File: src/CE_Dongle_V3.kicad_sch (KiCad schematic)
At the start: 6 parts, among them J2 8P8C_LED_Shielded

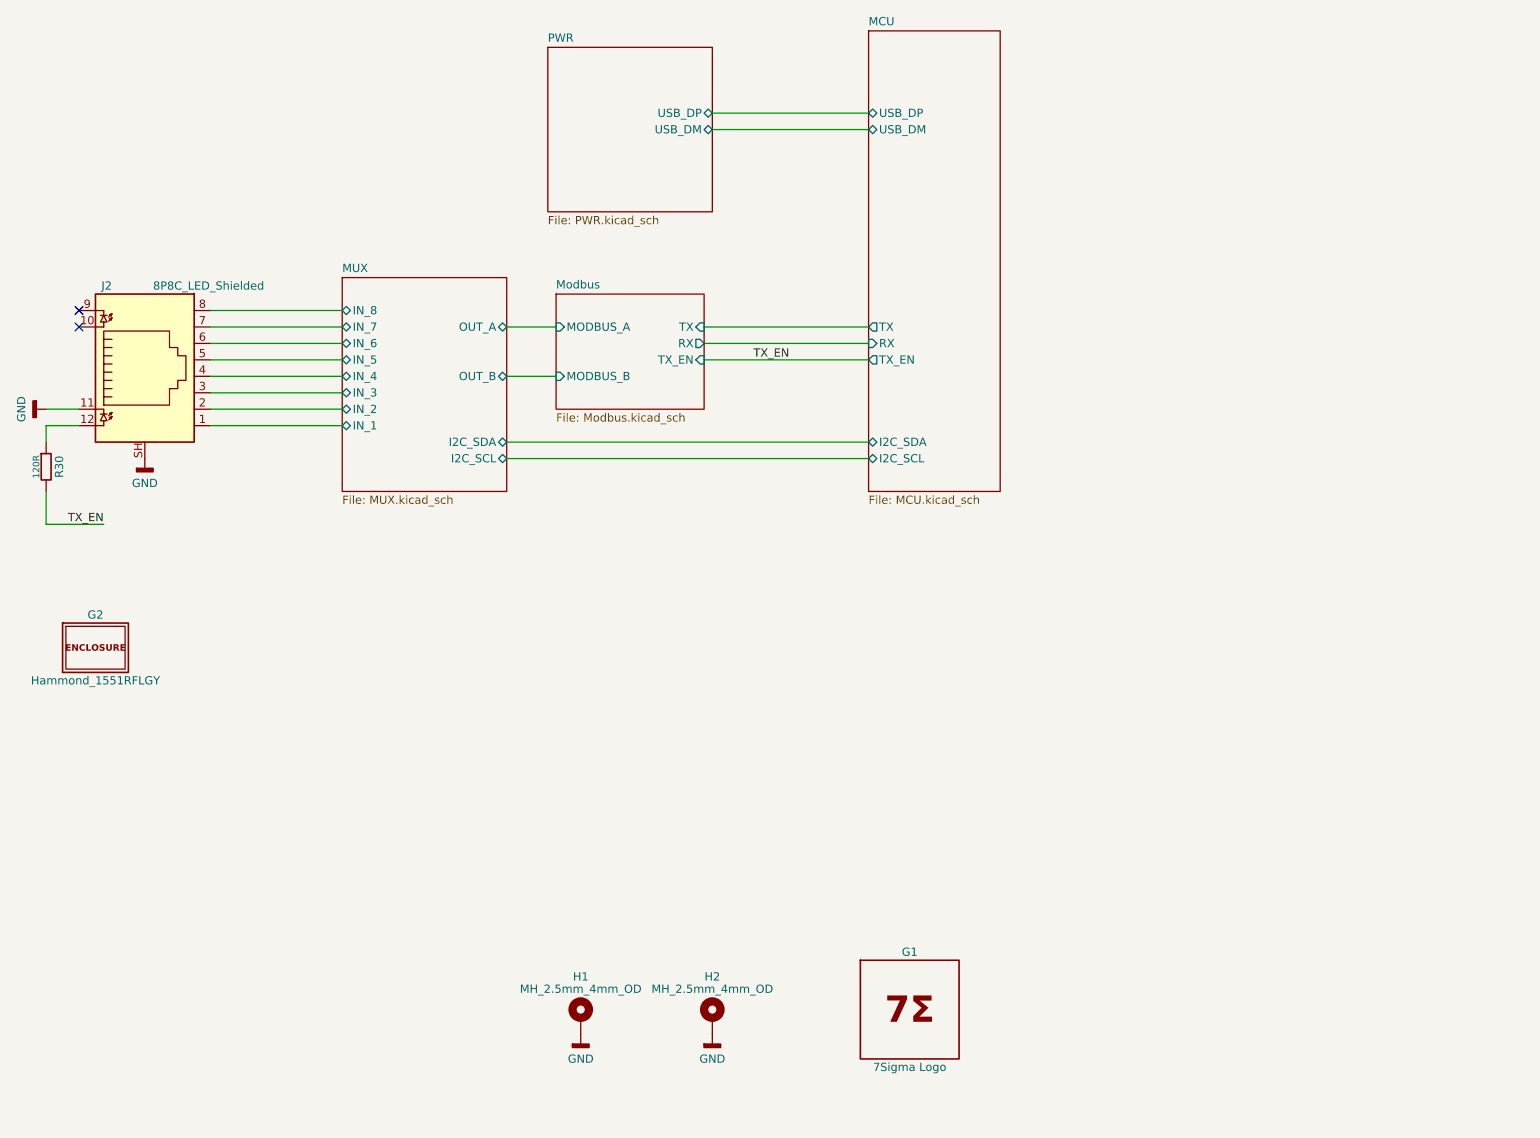
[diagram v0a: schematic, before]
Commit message: V3.1 first changes
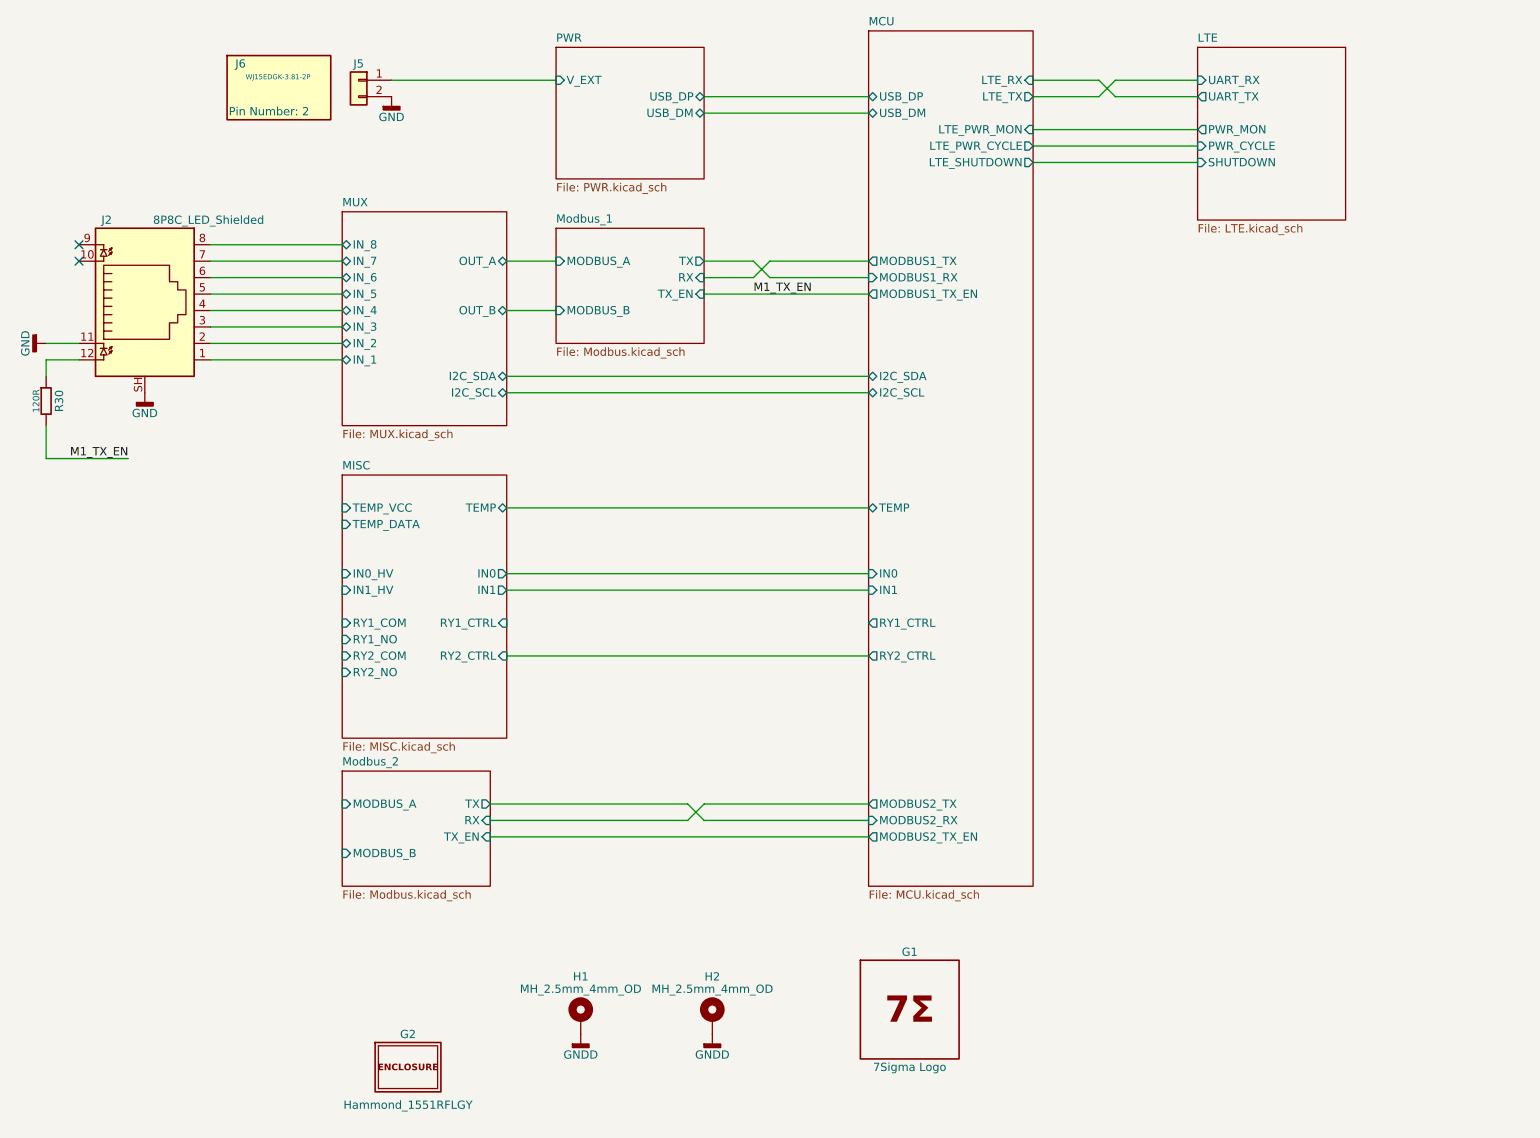
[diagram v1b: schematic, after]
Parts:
- added J5: Conn_01x02, 7Sigma:PhoenixContact_MC_1,5_2-G-3.81_1x02_P3.81mm_Horizontal, symbol Connectors:WJ15EDGRC-3.81-2P
- added J6: WJ15EDGK-3.81-2P, 7Sigma:TerminalBlock_Plug_Invisible, symbol Connectors:WJ15EDGK-3.81-2P
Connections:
- net GND: now also J5.2 (Pin_2); no longer H1.1, H2.1
- net TX_EN renamed M1_TX_EN
- new net GNDD: H1.1, H2.1
- new net PWR/V_EXT: J5.1 (Pin_1)
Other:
- sheet Modbus renamed Modbus_1
- added sheet LTE (LTE.kicad_sch)
- added sheet MISC (MISC.kicad_sch)
- added sheet Modbus_2 (Modbus.kicad_sch)
- sheet MCU ports: added IN0, IN1, LTE_PWR_CYCLE, LTE_PWR_MON, LTE_RX, LTE_SHUTDOWN, LTE_TX, MODBUS1_RX, MODBUS1_TX, MODBUS1_TX_EN, MODBUS2_RX, MODBUS2_TX, MODBUS2_TX_EN, RY1_CTRL, RY2_CTRL, TEMP; removed RX, TX, TX_EN
- sheet PWR ports: added V_EXT; removed none
- moved on the sheet: G2, J2, R30

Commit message: ongoing work
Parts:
- removed G2: Hammond_1551RFLGY, 7Sigma:HAMMOND_1551RFLGY, symbol Mechanical_7S:Hammond_1551RFLGY
- removed J2: 8P8C_LED_Shielded, 7Sigma:RJ45-TH_RC01812, symbol Connectors:RC01812
- removed J5: Conn_01x02, 7Sigma:PhoenixContact_MC_1,5_2-G-3.81_1x02_P3.81mm_Horizontal, symbol Connectors:WJ15EDGRC-3.81-2P
- removed J6: WJ15EDGK-3.81-2P, 7Sigma:TerminalBlock_Plug_Invisible, symbol Connectors:WJ15EDGK-3.81-2P
- removed R30: 120R, 7Sigma:R_0402_1005Metric, symbol Resistor:0402WGF1200TCE
- added ENC1: Hammond_1551XFLGY, 7Sigma:HAMMOND_1551XFLGY, symbol Mechanical_7S:Hammond_1551XFLGY
- added H3, H4: MH_2.5mm_4mm_OD, 7Sigma:MountingHole_2.5mm_Pad_4mm, symbol Mechanical_7S:MH_2.5mm_4mm_OD
- added J6: DB2EKDM-3.81-10P-GN, 7Sigma:TerminalBlock_Plug_Invisible, symbol Connectors:DB2EKDM-3.81-10P-GN
- added J7: 8P8C_LED_Shielded, 7Sigma:RJ45-TH_RC01812, symbol Connectors:RC01812
- added J8: DB2ERM-3.81-10P-GN, 7Sigma:PhoenixContact_MC_1,5_10-GF-3.81_1x10_P3.81mm_Horizontal_ThreadedFlange, symbol Connectors:DB2ERM-3.81-10P-GN
- added R29: 1K, 7Sigma:R_0402_1005Metric, symbol Resistor:0402WGF1001TCE
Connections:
- net GNDD is gone; now on net GND: H1.1, H2.1
- net GND: now also H3.1, H4.1, J7.SH, J8.3 (Pin_3), J8.8 (Pin_8), R29.2
- net MISC/RY1_COM: now also J8.4 (Pin_4)
- net MISC/RY1_NO: now also J8.5 (Pin_5)
- net MISC/RY2_NO: now also J8.6 (Pin_6)
- net MISC/TEMP_DATA: now also J8.2 (Pin_2)
- net MISC/TEMP_VCC: now also J8.1 (Pin_1)
- net MUX/IN_1: now also J7.1
- net MUX/IN_2: now also J7.2
- net MUX/IN_3: now also J7.3
- net MUX/IN_4: now also J7.4
- net MUX/IN_5: now also J7.5
- net MUX/IN_6: now also J7.6
- net MUX/IN_7: now also J7.7
- net MUX/IN_8: now also J7.8
- net MUX/OUT_A: now also J8.9 (Pin_9)
- net MUX/OUT_B: now also J8.10 (Pin_10)
- net PWR/V_EXT: now also J8.7 (Pin_7)
- new net: J7.11, R29.1
- new net TX_EN: J7.12
- no-connect marks 2 -> 0
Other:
- removed sheet Modbus_2
- sheet MCU ports: added none; removed IN0, IN1, MODBUS2_RX, MODBUS2_TX, MODBUS2_TX_EN
- sheet MISC ports: added R1_CTRL, R2_CTRL; removed IN0, IN0_HV, IN1, IN1_HV, RY1_CTRL, RY2_CTRL
- moved on the sheet: G1, H1, H2

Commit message: Layout progress
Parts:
- removed J6: DB2EKDM-3.81-10P-GN, 7Sigma:TerminalBlock_Plug_Invisible, symbol Connectors:DB2EKDM-3.81-10P-GN
- removed J8: DB2ERM-3.81-10P-GN, 7Sigma:PhoenixContact_MC_1,5_10-GF-3.81_1x10_P3.81mm_Horizontal_ThreadedFlange, symbol Connectors:DB2ERM-3.81-10P-GN
- added J10, J2, J3, J6, J8: Conn_01x02, 7Sigma:CONN-TH_DB301V-3.5-2P-GN, symbol Connectors:DB301V-3.5-2P-GN-S
- ENC1: Manufacturer 1 (none) -> FIX&Hammond Mfg; Manufacturer Part Number 1 (none) -> 1551XFLGY; Price @Bulk USD (none) -> 2.3700; Price Source (none) -> Manual
- J7: Price @1 USD (none) -> 0.5973; Price @100 USD (none) -> 0.3342; Price @Bulk USD (none) -> 0.2890; Price Bulk Qty (none) -> 1000; Price Source (none) -> LCSC; Price Updated (none) -> 2026-05-14
- R29: Price @1 USD (none) -> 0.0011; Price @100 USD (none) -> 0.0011; Price @Bulk USD (none) -> 0.0009; Price Bulk Qty (none) -> 1000; Price Source (none) -> LCSC; Price Updated (none) -> 2026-05-14
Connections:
- net GND: now also J3.1 (Pin_1), J8.2 (Pin_2)
- net MISC/RY1_COM: now also J3.2 (Pin_2)
- net MISC/RY1_NO: now also J6.1 (Pin_1)
- net MISC/RY2_NO: now also J6.2 (Pin_2)
- net MISC/TEMP_DATA: now also J2.2 (Pin_2)
- net MISC/TEMP_VCC: now also J2.1 (Pin_1)
- net MUX/OUT_A: now also J10.1 (Pin_1)
- net MUX/OUT_B: now also J10.2 (Pin_2)
- net PWR/V_EXT: now also J8.1 (Pin_1)

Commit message: PCB layout continued
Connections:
- net MISC/RY1_COM: now also J6.1 (Pin_1); no longer J3.2 (Pin_2)
- net MISC/RY1_NO: now also J3.2 (Pin_2); no longer J6.1 (Pin_1)
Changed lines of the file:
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@@
 	(paper "A4")
 	(junction
-		(at 101.6 66.04)
+		(at 127 104.14)
 		(diameter 0)
 		(color 0 0 0 0)
 	)
 	(junction
-		(at 127 101.6)
+		(at 101.6 66.04)
 		(diameter 0)
 		(color 0 0 0 0)
@@
 	(wire
 		(pts
-			(xy 129.54 104.14) (xy 127 104.14)
+			(xy 129.54 106.68) (xy 127 106.68)
 		)
 		(stroke
@@
 	(wire
 		(pts
-			(xy 127 101.6) (xy 129.54 101.6)
+			(xy 127 104.14) (xy 129.54 104.14)
 		)
 		(stroke
@@
 	(wire
 		(pts
-			(xy 139.7 60.96) (xy 162.56 60.96)
+			(xy 86.36 101.6) (xy 129.54 101.6)
 		)
 		(stroke
@@
 	(wire
 		(pts
-			(xy 35.56 71.12) (xy 33.02 71.12)
+			(xy 139.7 60.96) (xy 162.56 60.96)
 		)
 		(stroke
@@
 	(wire
 		(pts
-			(xy 86.36 101.6) (xy 127 101.6)
+			(xy 35.56 71.12) (xy 33.02 71.12)
 		)
 		(stroke
@@
 	(wire
 		(pts
-			(xy 124.46 104.14) (xy 86.36 104.14)
-		)
-		(stroke
-			(width 0)
-			(type default)
-		)
-	)
-	(wire
-		(pts
 			(xy 93.98 66.04) (xy 101.6 66.04)
 		)
@@
 	(wire
 		(pts
-			(xy 129.54 106.68) (xy 124.46 106.68)
+			(xy 86.36 104.14) (xy 127 104.14)
 		)
 		(stroke
@@
 	(wire
 		(pts
-			(xy 127 104.14) (xy 127 101.6)
+			(xy 127 106.68) (xy 127 104.14)
 		)
 		(stroke
@@
 	(wire
 		(pts
-			(xy 124.46 106.68) (xy 124.46 104.14)
-		)
-		(stroke
-			(width 0)
-			(type default)
-		)
-	)
-	(wire
-		(pts
 			(xy 101.6 116.84) (xy 101.6 66.04)
 		)
@@
 		)
 		(pin "RY1_COM" input
-			(at 129.54 101.6 180)
+			(at 129.54 104.14 180)
 			(effects
 				(font
@@
 		)
 		(pin "RY2_COM" input
-			(at 129.54 104.14 180)
+			(at 129.54 106.68 180)
 			(effects
 				(font
@@
 		)
 		(pin "RY1_NO" input
-			(at 129.54 106.68 180)
+			(at 129.54 101.6 180)
 			(effects
 				(font
